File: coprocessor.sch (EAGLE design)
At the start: 39 parts, among them IC1 MEGA32U2, J1 AVR_SPI_PRG_6NS

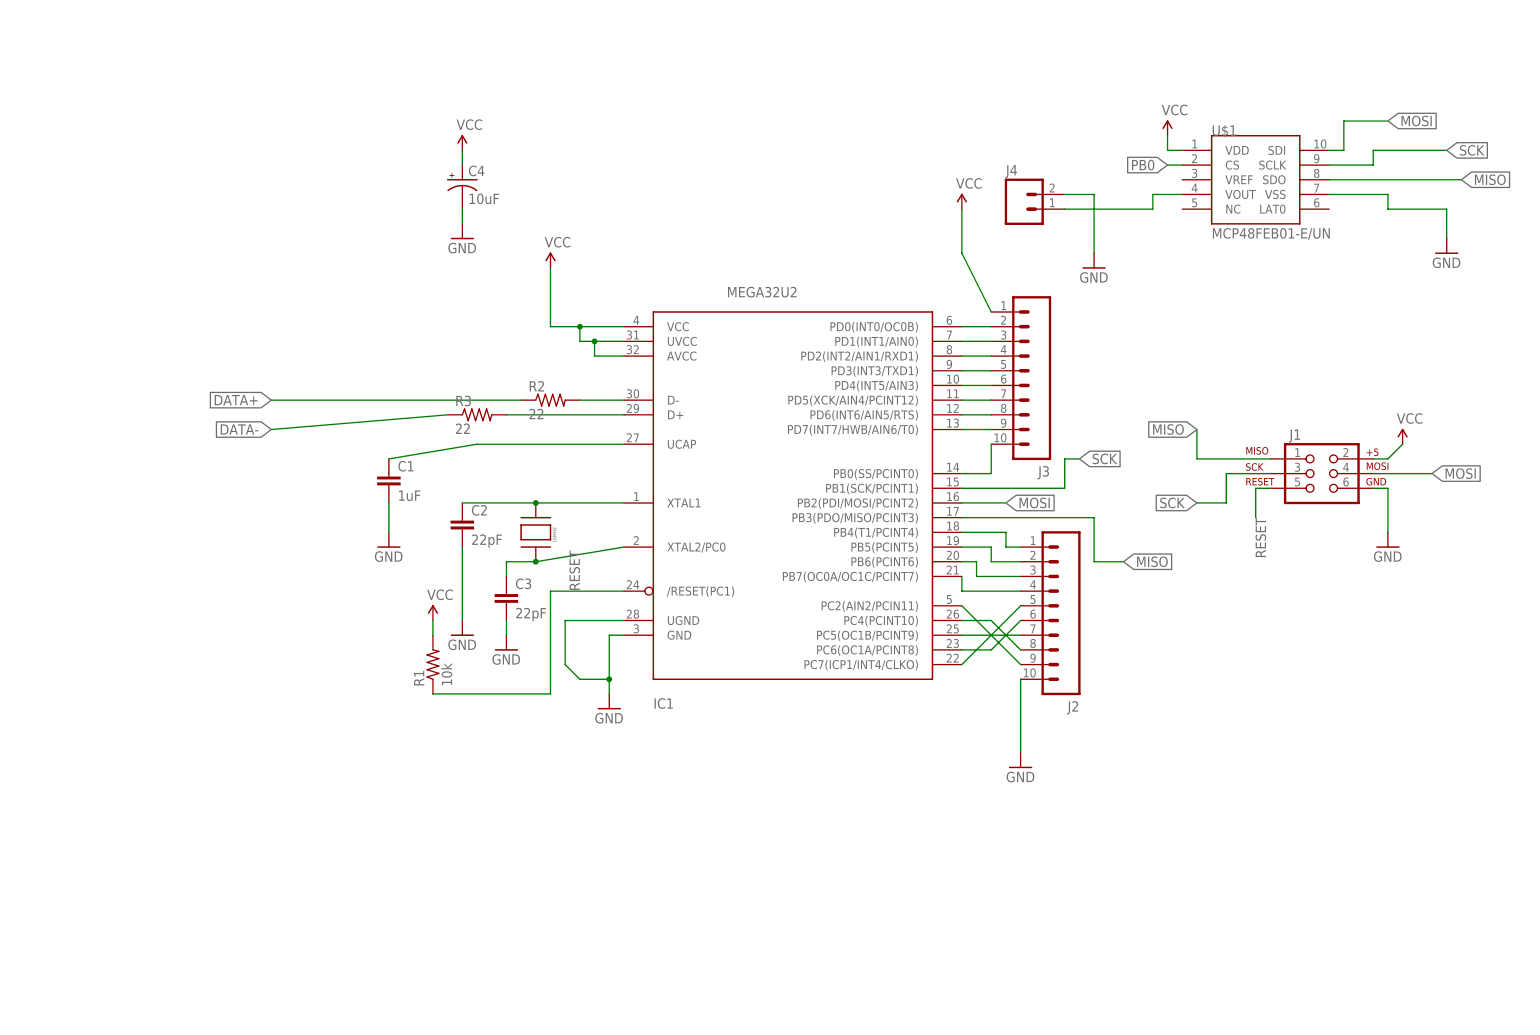
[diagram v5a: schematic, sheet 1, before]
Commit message: Added a few parts to the custom lib and added more to the coprocessor
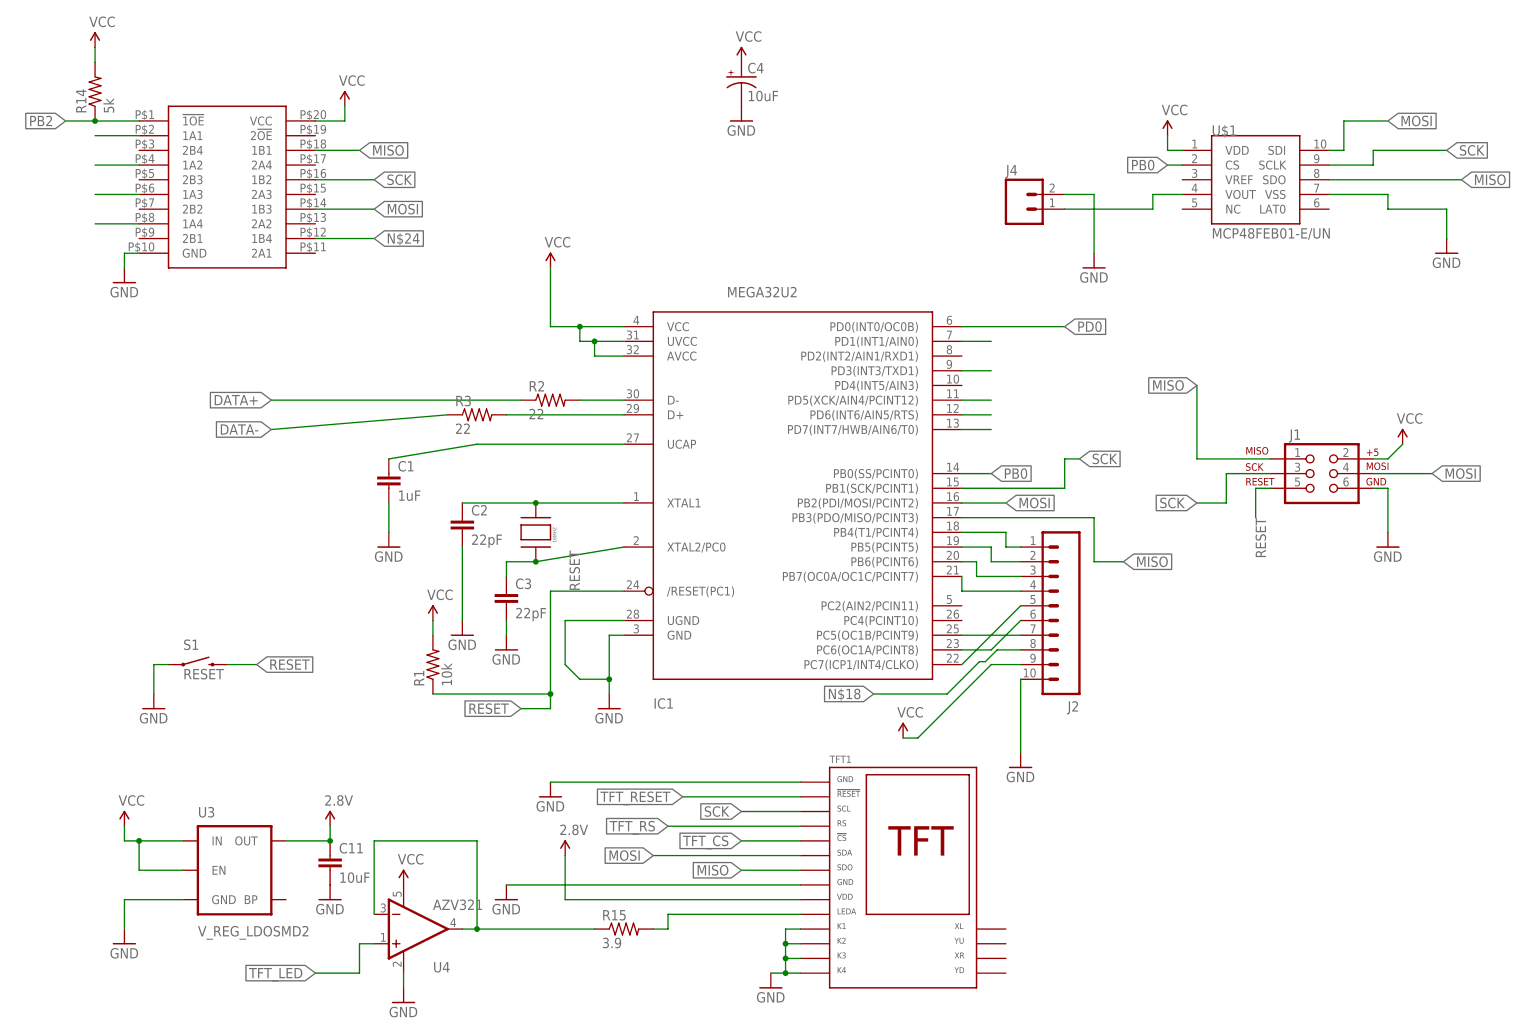
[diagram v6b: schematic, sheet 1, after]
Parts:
- removed FRAME2: FRAME-LETTERNO_PACKAGE, SparkFun-Aesthetics:FRAME-LETTERNO_PACKAGE
- removed J3: (no value), SparkFun-Connectors:M102MM
- added C11: 10uF, SparkFun-Capacitors:10UF10V10%(0805)
- added R14: 5k, SparkFun-Resistors:RESISTOR0805-RES
- added R15: 3.9, SparkFun-Resistors:RESISTOR0805-RES
- added S1: RESET, SparkFun-Electromechanical:SWITCH-MOMENTARY-2SMD
- added TFT1: TFT-18-1.0MM, custom:TFT-18-1.0MM
- added U$3: CBT3244AD, custom:CBT3244AD
- added U3: V_REG_LDOSMD2, SparkFun-PowerIC:V_REG_LDOSMD2
- added U4: AZV321, custom:AZV321
- C4: device SparkFun-Capacitors:CAP_POLSMD -> SparkFun-Capacitors:CAP_POL1206
- L1: device SparkFun-Coils:INDUCTOR-SDR13-27UH -> custom:MICROBUILDER_INDUCTORNR5040
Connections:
- removed net PC2: IC1.PC2(AIN2/PCIN11), J2.9
- removed net PC4: IC1.PC4(PCINT10), J2.8
- removed net PD2: IC1.PD2(INT2/AIN1/RXD1), J3.4
- removed net PD4: IC1.PD4(INT5/AIN3), J3.6
- new net 2.8V: C11.1, TFT1.VDD, U3.OUT
- new net N$18: J2.8
- new net N$19: R15.2, TFT1.LEDA
- new net N$20: R15.1, U4.-IN, U4.OUT
- new net N$24: U$3.1B4
- new net N$25: U$3.1A2
- new net N$26: U$3.1A3
- new net N$27: U$3.1A4
- new net N$5: U$3.1A1
- new net PB2: R14.1, U$3.!1OE
- new net TFT_CS: TFT1.!CS
- new net TFT_LED: U4.+IN
- new net TFT_RESET: TFT1.!RESET
- new net TFT_RS: TFT1.RS
- net GND: now also C11.2, S1.1, TFT1.GND@1, TFT1.GND@2, TFT1.K1, TFT1.K2, TFT1.K3, TFT1.K4, U$3.GND, U3.GND, U4.V-
- net MISO: now also TFT1.SDO, U$3.1B1
- net MOSI: now also TFT1.SDA, U$3.1B3
- net PB0: no longer J3.10
- net PD0: no longer J3.2
- net PD1: no longer J3.3
- net PD3: no longer J3.5
- net PD5: no longer J3.7
- net PD6: no longer J3.8
- net PD7: no longer J3.9
- net RESET: now also S1.2
- net SCK: now also TFT1.SCL, U$3.1B2
- net VCC: now also J2.9, R14.2, U$3.VCC, U3.EN, U3.IN, U4.V+; no longer J3.1
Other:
- moved on the sheet: C4

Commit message: Added a cool logo
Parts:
- added FRAME2: FRAME-LETTER, SparkFun-Aesthetics:FRAME-LETTER
- added LED1: DONE, adafruit:LEDCHIPLED_0603
- added LED2: CHG, adafruit:LEDCHIPLED_0603
- added R16, R17: 1K, SparkFun-Resistors:1KOHM-1/10W-1%(0603)
- added THERM: 16k, SparkFun-Resistors:RESISTOR0603-RES
- C10: value (none) -> 100uF
- R4: value 340 -> 340k
- R5, R7: value 1.86m -> 1.87M
- U1: value (none) -> TPS61090RSAR
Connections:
- removed net PB4: IC1.PB4(T1/PCINT4), J2.1
- removed net PB5: IC1.PB5(PCINT5), J2.2
- removed net PB6: IC1.PB6(PCINT6), J2.3
- removed net PB7: IC1.PB7(OC0A/OC1C/PCINT7), J2.4
- removed net PC5: IC1.PC5(OC1B/PCINT9), J2.7
- removed net PC6: IC1.PC6(OC1A/PCINT8), J2.6
- removed net PC7: IC1.PC7(ICP1/INT4/CLKO), J2.5
- removed net PD1: IC1.PD1(INT1/AIN0)
- removed net PD3: IC1.PD3(INT3/TXD1)
- new net N$21: R17.1, U2.STAT1/LBO
- new net N$22: LED1.C, R16.2
- new net N$23: LED2.C, R17.2
- net GND: now also THERM.1; no longer J2.10
- net MISO: no longer U$3.1B1
- net N$18: now also R16.1, U2.STAT2; no longer J2.8
- net N$24: now also THERM.2, U2.THERM; no longer U$3.1B4
- net TFT_CS: now also IC1.PD3(INT3/TXD1), U$3.1B1
- net TFT_LED: now also IC1.PD1(INT1/AIN0)
- net TFT_RS: now also IC1.PD2(INT2/AIN1/RXD1), U$3.1B4
- net VCC: no longer J2.9
- net V_USB: now also LED1.A, LED2.A
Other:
- note added: "5v to 2.8v converter for LCD"
- note added: "Audio DAC"
- note added: "Battery controller"
- note added: "Boost converter"
- note added: "Bus switch"
- note added: "Programming header"
- note added: "TFT Screen"
- note added: "USB Connector"
- moved on the sheet: C10, C11, C5, C6, C7, C9, D2, L1, R10, R13, R4, R5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

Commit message: Added some aesthetics
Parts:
- FRAME2: value FRAME-LETTER -> Matthew Carlson
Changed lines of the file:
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@@
 <schematic xreflabel="%F%N/%S.%C%R" xrefpart="/%S.%C%R">
 <attributes>
+<attribute name="CREVISION" value="0.2"/>
+<attribute name="DESIGNER" value="Matthew Carlson"/>
 </attributes>
 <variantdefs>
@@
 <part name="THERM" library="SparkFun-Resistors" deviceset="RESISTOR" device="0603-RES" value="16k"/>
 <part name="GND7" library="SparkFun-Aesthetics" deviceset="GND" device=""/>
-<part name="FRAME2" library="SparkFun-Aesthetics" deviceset="FRAME-LETTER" device=""/>
+<part name="FRAME2" library="SparkFun-Aesthetics" deviceset="FRAME-LETTER" device="" value="Matthew Carlson"/>
 </parts>
 <sheets>
